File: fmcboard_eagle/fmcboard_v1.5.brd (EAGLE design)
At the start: 147 x 74 mm, 174 parts, among them IC1 OPA699ID, IC10 LTC6229IMS8E#TRPBF, IC11 7805TV, IC12 SN74AUC2G66DCTR, IC13 SN74AUC2G66DCTR, IC14 SN74AUC2G66DCTR, IC15 SN74AUC2G66DCTR, IC16 DAC7578SPWR, IC17 SN74AUC2G66DCTR, IC18 SN74AUC2G66DCTR, IC19 SN74AUC2G66DCTR, IC2 DAC7578SPWR, IC20 SN74AUC2G66DCTR, IC21 74AUP2GU04GW,125, IC22 74AUP2GU04GW,125, IC23 74AUP2GU04GW,125, IC24 74AUP2GU04GW,125, IC3 LTC6229IMS8E#TRPBF, IC4 LTC6229IMS8E#TRPBF, IC5 LM358, IC6 OPA699ID, IC7 OPA699ID, IC8 LTC6229IMS8E#TRPBF, IC9 LTC6229IMS8E#TRPBF, J1 8pin, J10 8pin, J12 4p-2.54, J2 ASP-134604-01, J3 4p-2.54, J4 4p-2.54, J5 8pin, J6 4p-2.54, J7 4p-2.54, J8 4p-2.54, J9 8pin, U1 TXS0108EPWR, U2 STMICROELECTRONICS_L7905ACVST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

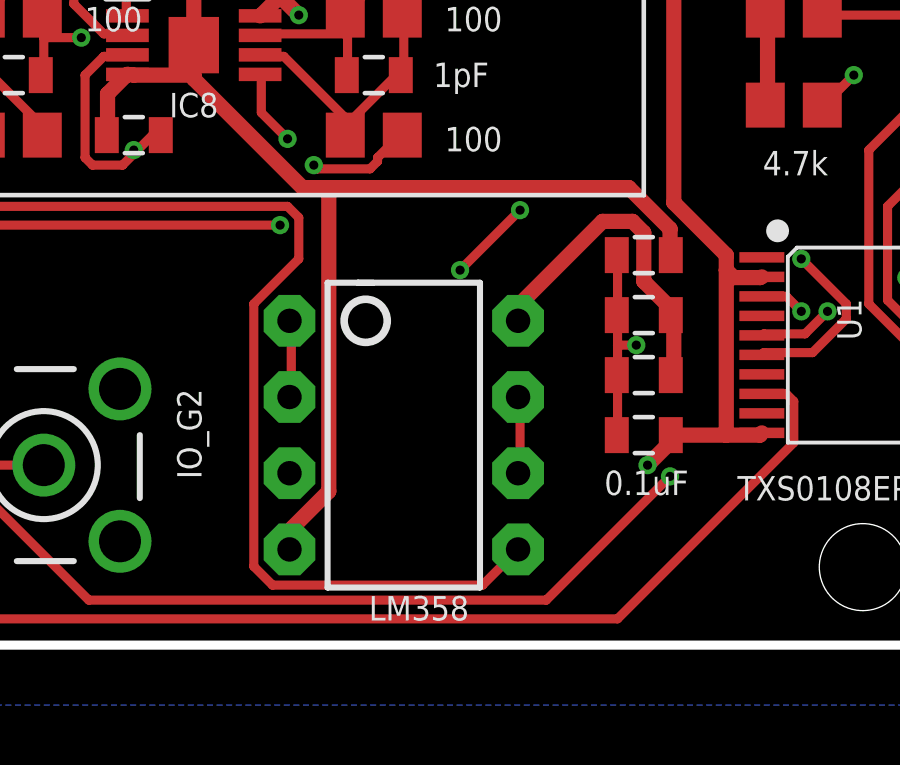
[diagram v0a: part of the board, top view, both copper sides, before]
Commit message: Use SMT LM358
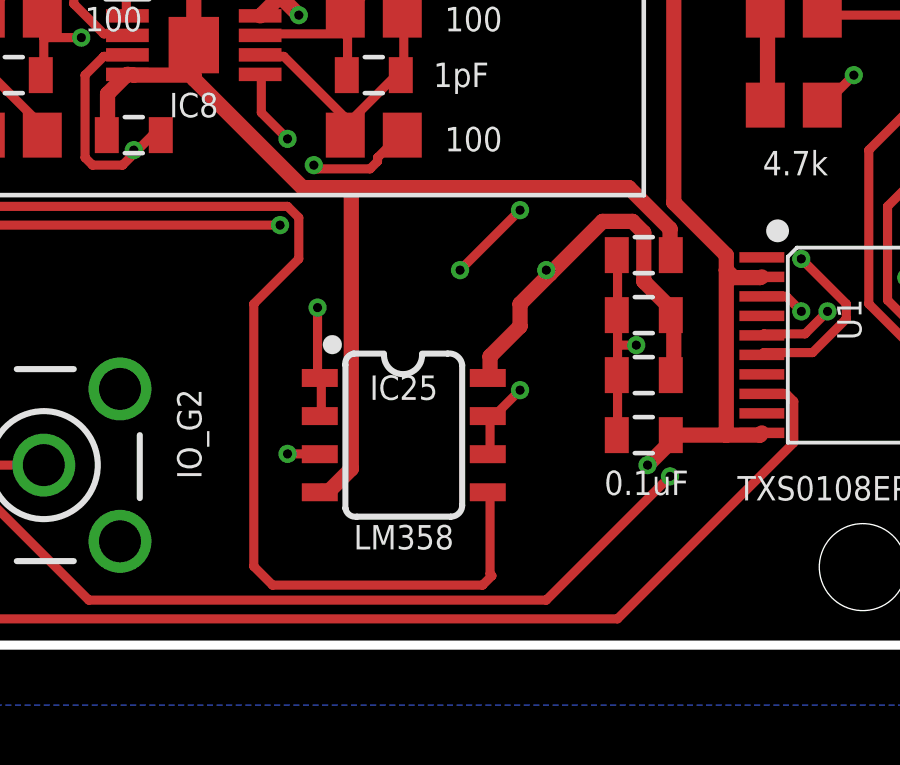
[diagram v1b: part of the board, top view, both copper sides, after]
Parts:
- removed IC5: LM358, SparkFun-AnalogIC:DIP08
- added IC25: LM358, SparkFun-IC-Amplifiers:SO08
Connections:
- net OFFSETIN1: now also IC25.3; no longer IC5.3
- net OFFSETIN2: now also IC25.5; no longer IC5.5
- net OFFSETOUT1: now also IC25.1, IC25.2; no longer IC5.1, IC5.2
- net OFFSETOUT2: now also IC25.6, IC25.7; no longer IC5.6, IC5.7
- net VS+: now also IC25.8; no longer IC5.8
- net VS-: now also IC25.4; no longer IC5.4
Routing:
- net VS-: track 342.6 -> 340.7 mm
- net OFFSETIN2: track 100.5 -> 102.1 mm
- net VS+: track 374.9 -> 376.0 mm, vias 13 -> 14
- net OFFSETOUT1: track 33.4 -> 34.5 mm, vias 1 -> 2
- net OFFSETIN1: track 98.9 -> 99.5 mm, vias 3 -> 4
- net OFFSETOUT2: vias 1 -> 2

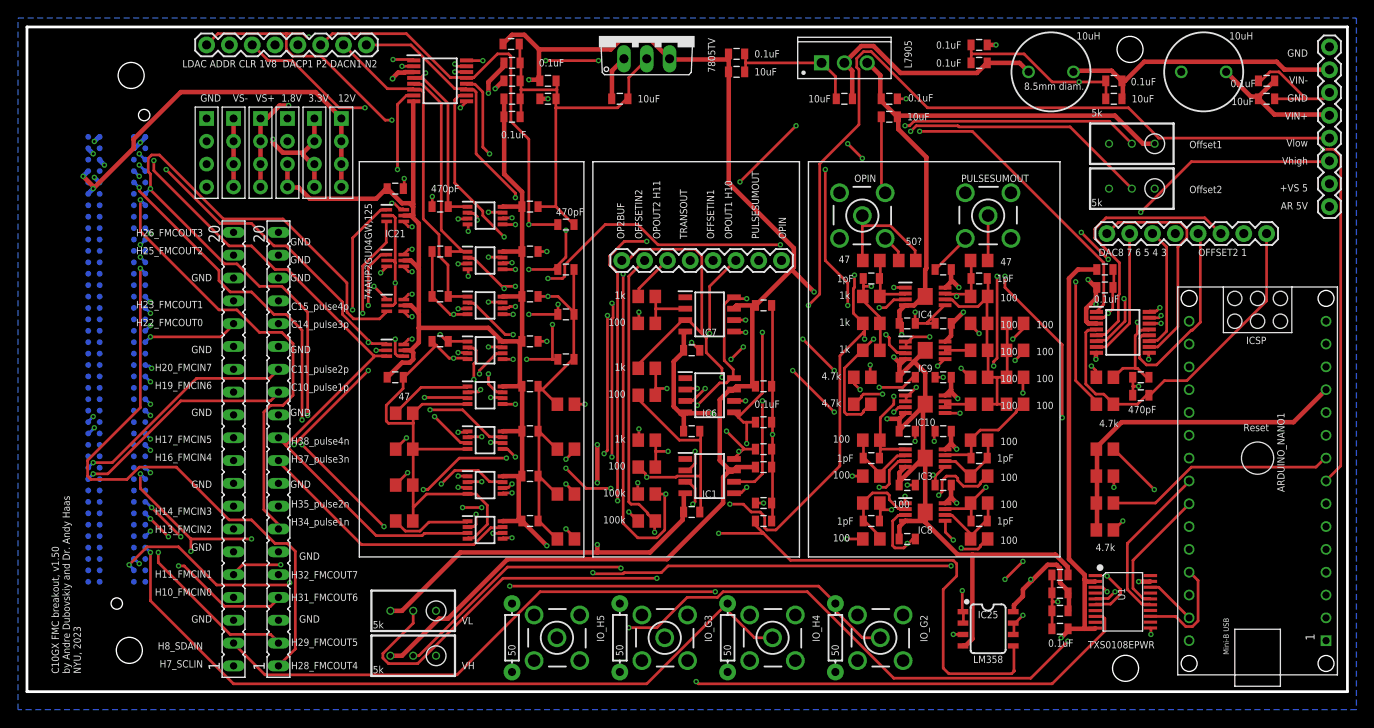
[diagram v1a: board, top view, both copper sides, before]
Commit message: v1.51 : Add 1k resistors before DAC caps (to prevent oscillations), and make the caps 470pF -> 1uF
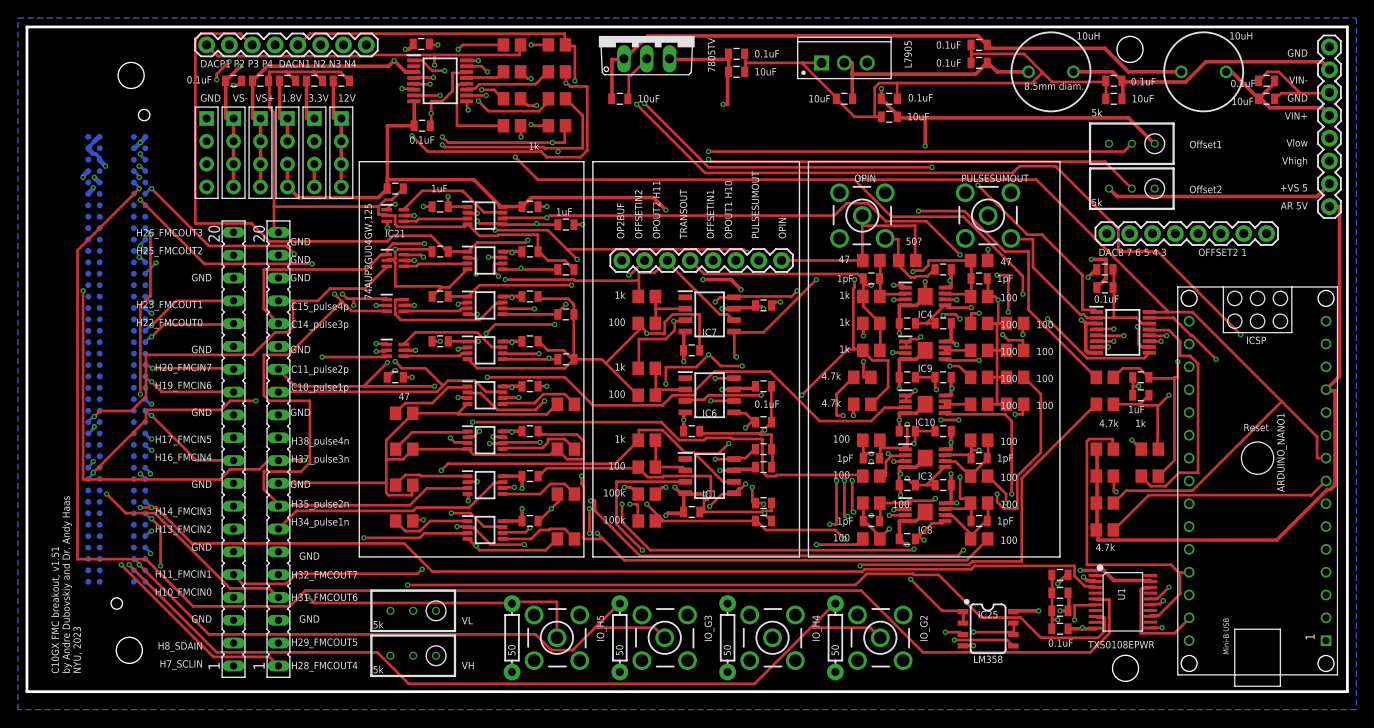
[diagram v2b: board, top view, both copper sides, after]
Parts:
- added R47, R53, R54, R55, R56, R57, R58, R59, R60, R61: 1k, rcl:R0805
- C56, C57, C58, C59, C60, C61, C62, C63, C64, C65: value 470pF -> 1uF
- moved C10 35.1 mm to (23.0, 68.0)
- moved C3 32.0 mm to (26.0, 68.0)
- moved C5 25.1 mm to (29.0, 68.0)
- moved C13 22.0 mm to (32.0, 68.0)
- moved C12 19.1 mm to (35.0, 68.0)
- moved C49 10.0 mm to (44.0, 63.0)
- moved C48 10.0 mm to (43.9, 72.1)
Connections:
- new net N$21: IC2.13, R56.2
- new net N$22: IC2.4, R47.1
- new net N$23: IC2.5, R53.1
- new net N$24: IC2.6, R54.1
- new net N$25: IC2.7, R55.1
- new net N$26: IC2.12, R57.2
- new net N$27: IC2.11, R58.2
- new net N$28: IC2.10, R59.2
- new net N$29: IC16.4, R60.1
- new net N$30: IC16.13, R61.2
- net 1V8: no longer J9.4
- net DACADDR: no longer J9.2
- net DACCLR: no longer J9.3
- net DACLDAC: no longer J9.1
- net DACN1: now also J9.5, R54.2; no longer IC2.6, J9.7
- net DACN2: now also J9.6, R58.1; no longer IC2.11, J9.8
- net DACN3: now also J9.7, R55.2; no longer IC2.7
- net DACN4: now also J9.8, R59.1; no longer IC2.10
- net DACOFFSET1: now also R60.2; no longer IC16.4
- net DACOFFSET2: now also R61.1; no longer IC16.13
- net DACP1: now also J9.1, R47.2; no longer IC2.4, J9.5
- net DACP2: now also J9.2, R56.1; no longer IC2.13, J9.6
- net DACP3: now also J9.3, R53.2; no longer IC2.5
- net DACP4: now also J9.4, R57.1; no longer IC2.12
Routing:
- net GND: track 397.7 -> 516.4 mm
- net DACP3: track 23.5 -> 85.0 mm, vias 0 -> 2
- net DACLDAC: track 133.9 -> 90.3 mm
- net AR_SCLIN2: track 179.3 -> 141.0 mm, vias 4 -> 2
- net DACN1: track 37.1 -> 73.7 mm, vias 0 -> 2
- net DACN3: track 35.4 -> 70.7 mm, vias 2 -> 5
- net AR_SDAIN2: track 191.0 -> 158.5 mm
- net DACCLR: track 119.9 -> 89.8 mm, vias 5 -> 4
- net DACN2: track 49.1 -> 78.5 mm, vias 4 -> 3
- net N$30: track 0.00 -> 27.6 mm
- net OFFSETIN2: track 102.1 -> 77.0 mm, vias 2 -> 4
- net DACP4: track 32.7 -> 56.8 mm, vias 4 -> 2
- net DACADDR: track 23.1 -> 0.00 mm, vias 1 -> 0
- net G37: track 150.7 -> 173.1 mm, vias 6 -> 2
- net DACP1: track 35.0 -> 57.2 mm, vias 1 -> 2
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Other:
- board text added: "C10GX FMC breakout, v1.51 by Andre Dubovskiy and Dr. Andy Haas NYU, 2023"
- board text added: "DACP1 P2 P3 P4 DACN1 N2 N3 N4"
- board text removed: "C10GX FMC breakout, v1.50 by Andre Dubovskiy and Dr. Andy Haas NYU, 2023"
- board text removed: "LDAC ADDR CLR 1V8 DACP1 P2 DACN1 N2"

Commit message: remove 47 ohm resistors to gnd
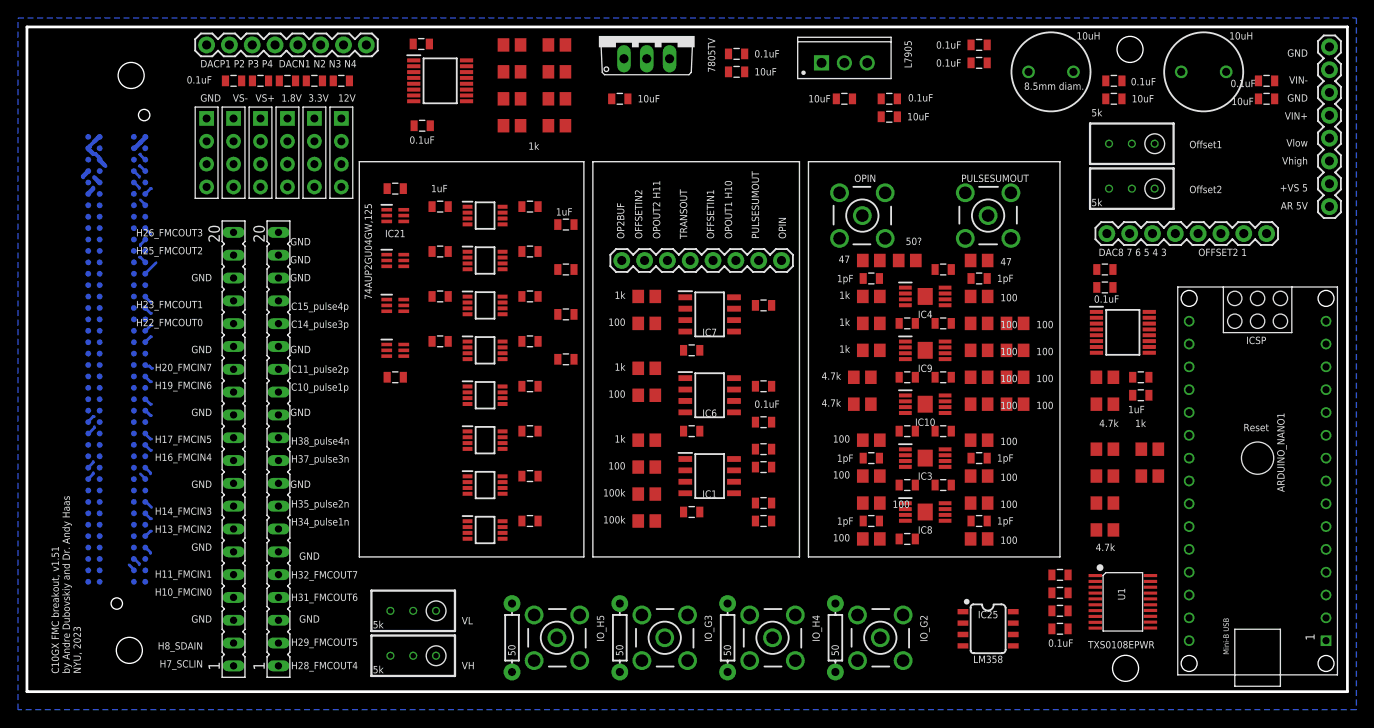
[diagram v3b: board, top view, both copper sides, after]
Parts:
- removed R37, R39, R41, R43, R44, R45, R46, R52: 47, rcl:R0805
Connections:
- removed net N$15: IC19.5, R41.2
- removed net N$16: IC20.5, R43.2
- removed net N$17: IC20.1, R44.1
- removed net N$19: IC19.1, R45.1
- removed net N$20: IC18.1, R46.1
- removed net N$5: IC17.1, R52.1
- removed net N$6: IC17.5, R37.2
- removed net N$7: IC18.5, R39.2
- net GND: now also IC17.1, IC17.5, IC18.1, IC18.5, IC19.1, IC19.5, IC20.1, IC20.5; no longer R37.1, R39.1, R41.1, R43.1, R44.2, R45.2, R46.2, R52.2
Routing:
- net GND: track 516.4 -> 1.54 mm, vias 34 -> 0
- net VS+: track 354.5 -> 0.00 mm, vias 18 -> 0
- net VS-: track 319.8 -> 0.00 mm, vias 17 -> 0
- net 1V8: track 304.3 -> 1.94 mm, vias 19 -> 0
- net G37: track 173.1 -> 0.96 mm, vias 2 -> 0
- net G36: track 171.9 -> 0.94 mm, vias 1 -> 0
- net AR_SDAIN2: track 158.5 -> 0.00 mm, vias 4 -> 0
- net VL: track 153.4 -> 0.00 mm, vias 5 -> 0
- net VH: track 149.7 -> 0.00 mm, vias 6 -> 0
- net AR_SCLIN2: track 141.0 -> 0.00 mm, vias 2 -> 0
- net SDAIN: track 131.9 -> 0.96 mm, vias 2 -> 0
- net SCLIN: track 128.7 -> 0.96 mm, vias 3 -> 0
- net N$1: track 112.3 -> 0.00 mm, vias 6 -> 0
- net OPOUT1_H10: track 112.6 -> 0.81 mm, vias 3 -> 0
- net PULSEINP4: track 105.6 -> 0.00 mm, vias 6 -> 0
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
